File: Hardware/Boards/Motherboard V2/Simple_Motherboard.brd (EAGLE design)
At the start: 146.1 x 147.3 mm, 120 parts, among them J1 AVR_SPI_PRG_6PTH, U1 WIZ811MJ, U1_MUX 74HC4052D,653, U2 ATMEGA328P_PDIP, U2_MUX 74HC4052D,653, U3_MUX 74HC4052D,653, U4_MUX 74HC4052D,653, U5_MUX 74HC4052D,653, U7_MUX 74HC4052D,653, Y1 16MHz

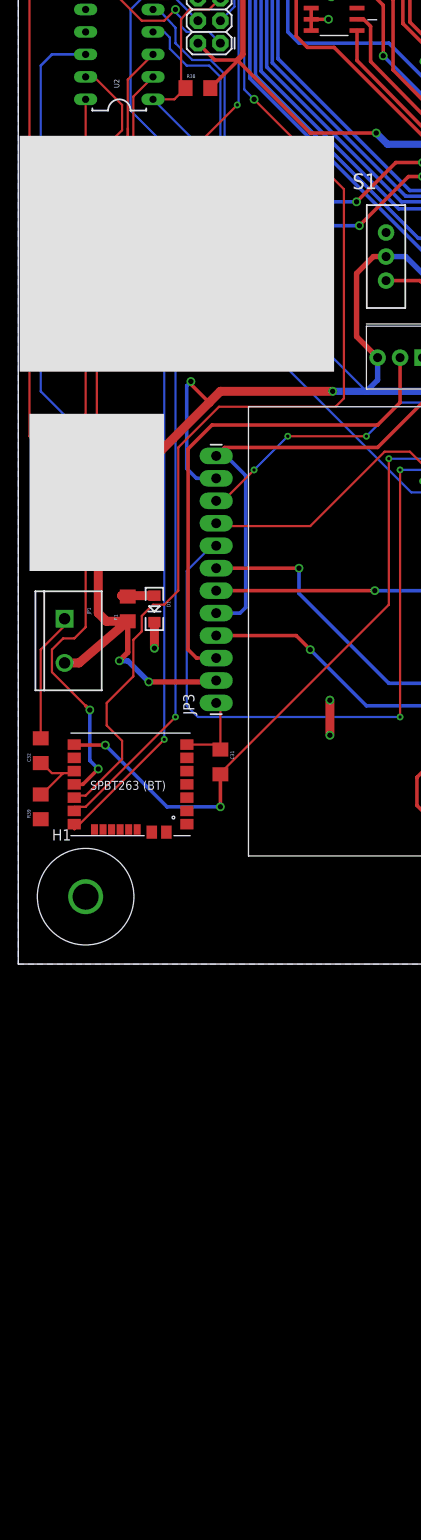
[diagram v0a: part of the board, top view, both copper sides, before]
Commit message: Removed sensor breakouts
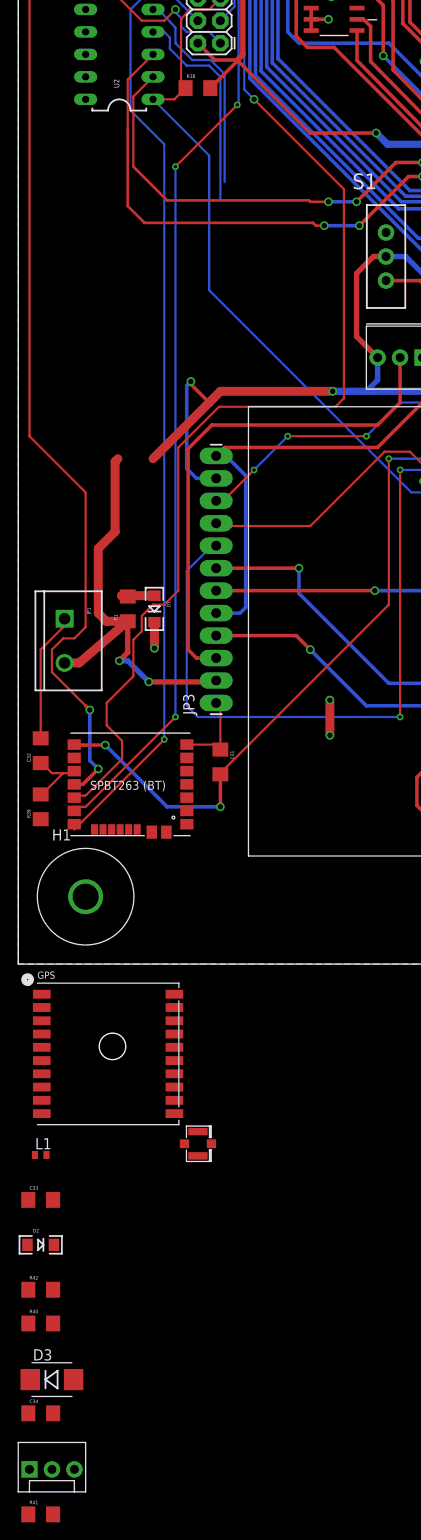
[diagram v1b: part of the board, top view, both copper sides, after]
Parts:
- removed JP2: (no value), SparkFun-Connectors:1X06_LONGPADS
- added C33: 1uF, SparkFun-Passives:1206
- added C34: .01uF, SparkFun-Passives:1206
- added D2: RED, SparkFun-LED:LED-1206
- added D3: (no value), SparkFun-DiscreteSemi:DIODE-HV
- added J2: U.FL, SparkFun-Connectors:U.FL
- added L1: BML15HB121SN1, inductors:0402
- added R40, R42: 1K, SparkFun-Passives:1206
- added R41: 10K, SparkFun-Passives:1206
- added TEMP: (no value), SparkFun-Connectors:MOLEX-1X3
- GPS: value M09 -> (none); device SparkFun-Connectors:1X09 -> adafruit:FGPMMOPA6H
- moved GPS 102.6 mm to (10.2, -10.2), turned to 0 degrees
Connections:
- removed net TMP_AL: JP2.4, U2.26
- removed net TMP_SCL: JP2.2, U2.28
- removed net TMP_SDA: JP2.1, U2.27
- new net N$23: D2.A, GPS.P$5
- new net N$24: D3.A, GPS.P$10, R40.1
- new net N$47: C33.1, C34.1, GPS.P$1, L1.2
- new net N$5: GPS.P$11, J2.P$3
- new net N$6: D2.C, R42.2
- new net TEMP: R41.1, TEMP.2, U2.23
- net +3V3: now also L1.1, R40.2
- net +5V: now also R41.2, TEMP.1; no longer GPS.8, JP2.5
- net GND: now also C33.2, C34.2, GPS.P$12, GPS.P$19, GPS.P$3, GPS.P$8, J2.P$1, J2.P$2, R42.1, TEMP.3; no longer GPS.7, JP2.6
- net GPS_RX: now also D3.C; no longer GPS.6
- net GPS_TX: now also GPS.P$9; no longer GPS.5
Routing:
- net TMP_SDA: track 59.6 -> 0.00 mm, vias 1 -> 0
- net TMP_AL: track 58.1 -> 0.00 mm
- net TMP_SCL: track 51.6 -> 0.00 mm, vias 1 -> 0
- net +5V: track 505.2 -> 490.5 mm
- net GPS_RX: track 37.0 -> 24.4 mm
- net GPS_TX: track 36.3 -> 24.4 mm

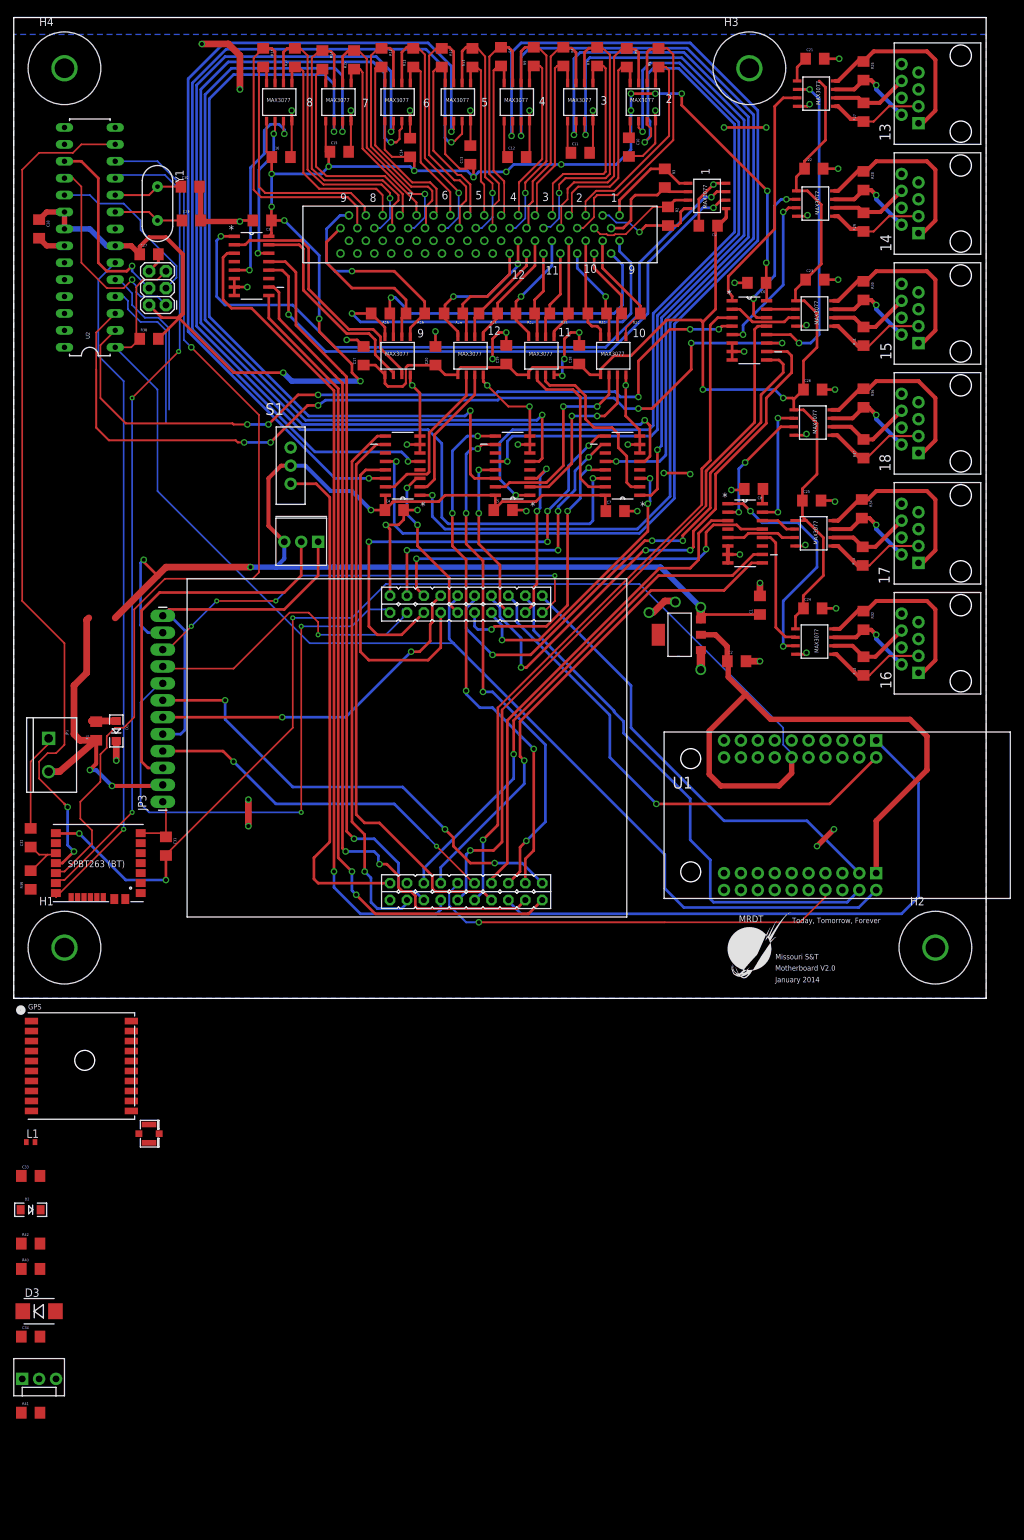
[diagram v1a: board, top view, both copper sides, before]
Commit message: Rewired LCD with 16 pin holes
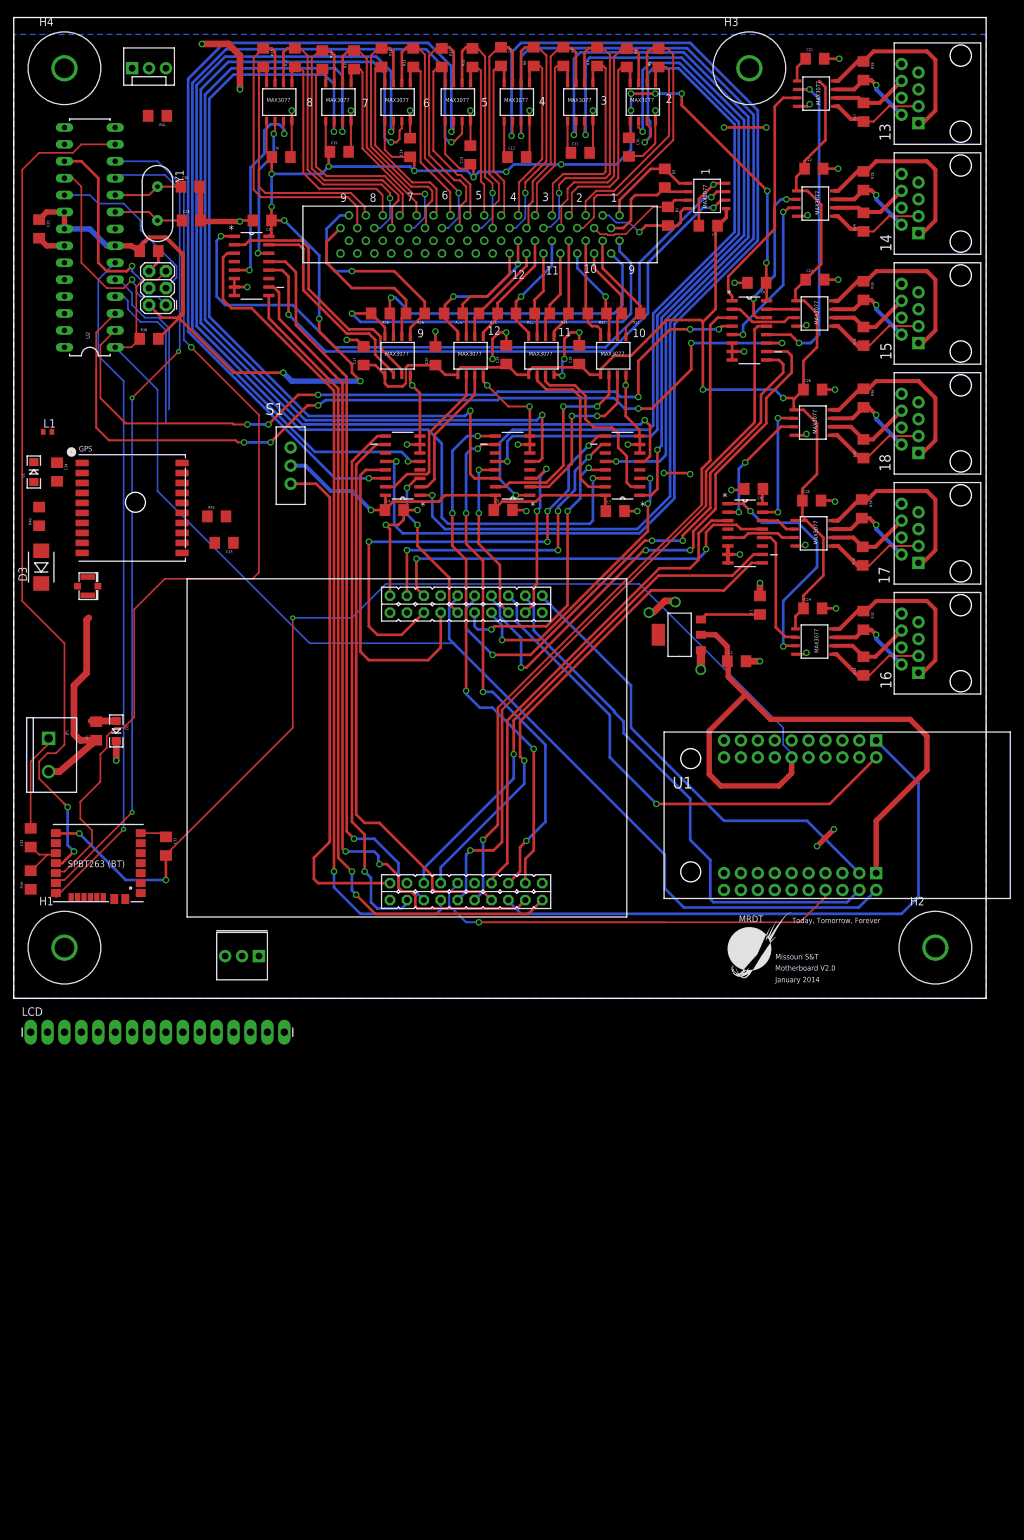
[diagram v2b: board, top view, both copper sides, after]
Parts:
- removed JP3: M12LONGPADS, SparkFun-Connectors:1X12_LONGPADS
- added LCD: M16LONGPADS, SparkFun-Connectors:1X16_LONGPADS
- moved TEMP 197.5 mm to (17.8, 139.7)
- moved R41 195.7 mm to (21.6, 132.6), turned to 180 degrees
- moved C34 129.9 mm to (6.51, 79.1), turned to 270 degrees
- moved R40 113.0 mm to (3.81, 72.4), turned to 90 degrees
- moved R42 112.7 mm to (30.5, 72.4)
- moved D3 111.8 mm to (4.13, 64.8), turned to 90 degrees
- moved D2 110.8 mm to (3.02, 79.1), turned to 90 degrees
- moved L1 106.7 mm to (5.08, 85.1)
- moved C33 99.4 mm to (31.6, 68.4), turned to 180 degrees
- moved GPS 84.2 mm to (17.8, 73.7)
- moved J2 82.7 mm to (11.1, 61.9)
- moved U$10 62.9 mm to (36.8, 8.89)
- moved C27 0.48 mm to (20.3, 112.2)
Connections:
- net +5V: now also LCD.15, LCD.2; no longer JP3.11, JP3.2
- net GND: now also LCD.1; no longer JP3.1
- net LCD_D4: now also LCD.11; no longer JP3.7
- net LCD_D5: now also LCD.12; no longer JP3.8
- net LCD_D6: now also LCD.13; no longer JP3.9
- net LCD_D7: now also LCD.14; no longer JP3.10
- net LCD_EN: now also LCD.6; no longer JP3.6
- net LCD_RS: now also LCD.4; no longer JP3.4
- net LCD_RW: now also LCD.16, LCD.5; no longer JP3.12, JP3.5
- net N$7: now also LCD.3; no longer JP3.3
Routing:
- net +5V: track 490.5 -> 342.3 mm, vias 23 -> 18
- net LCD_D5: track 86.8 -> 0.00 mm, vias 2 -> 0
- net LCD_D4: track 70.8 -> 0.00 mm, vias 3 -> 0
- net LCD_D7: track 70.1 -> 0.00 mm, vias 4 -> 0
- net N$7: track 57.5 -> 0.00 mm
- net LCD_RS: track 55.0 -> 0.00 mm, vias 2 -> 0
- net LCD_RW: track 53.7 -> 0.00 mm
- net LCD_EN: track 52.4 -> 0.00 mm, vias 2 -> 0
- net LCD_D6: track 45.2 -> 0.00 mm, vias 1 -> 0
- net GND: track 279.9 -> 270.9 mm, vias 60 -> 58

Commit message: Fixed some drc stuff
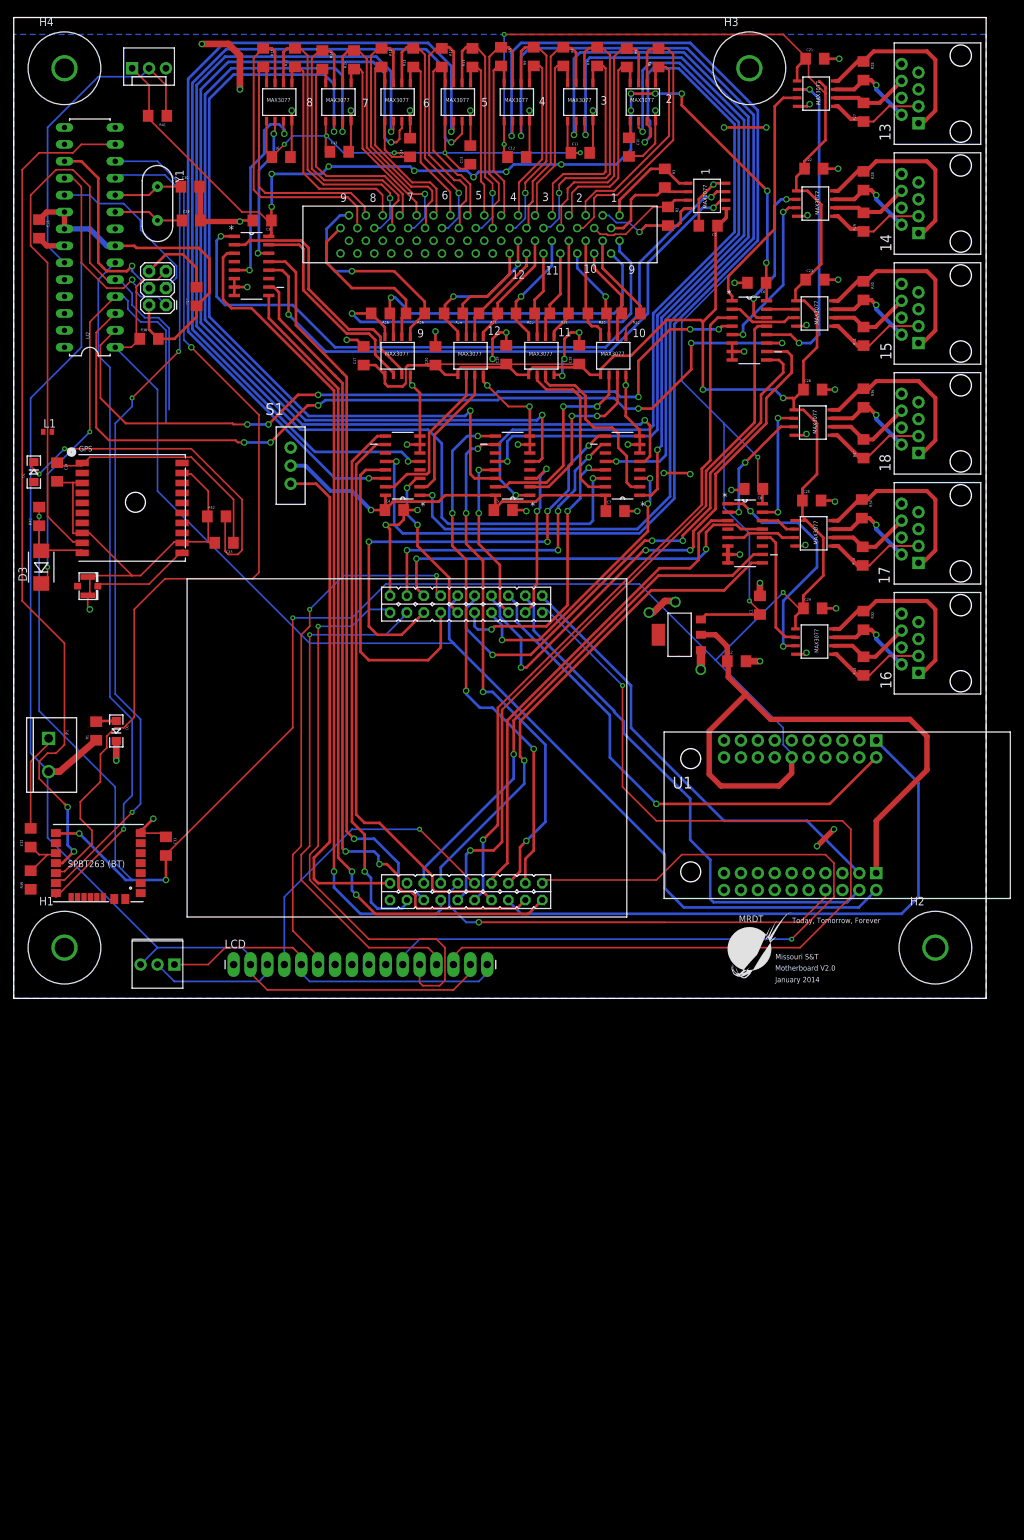
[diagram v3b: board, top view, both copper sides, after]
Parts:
- moved LCD 32.1 mm to (33.0, 5.08)
- moved U$10 12.8 mm to (24.1, 7.62)
- moved C27 9.88 mm to (27.5, 105.4), turned to 90 degrees
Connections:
- removed net LCD_RW: LCD.16, LCD.5, U$10.P$1
- net GND: now also LCD.16, LCD.5, U$10.P$1
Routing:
- net +3V3: track 509.6 -> 738.7 mm, vias 5 -> 14
- net +5V: track 342.3 -> 542.5 mm, vias 18 -> 16
- net LCD_D7: track 0.00 -> 143.9 mm, vias 0 -> 1
- net GND: track 270.9 -> 397.0 mm, vias 58 -> 60
- net LCD_D4: track 0.00 -> 120.9 mm, vias 0 -> 1
- net LCD_D5: track 0.00 -> 87.1 mm, vias 0 -> 1
- net GPS_TX: track 24.4 -> 108.4 mm
- net LCD_D6: track 0.00 -> 80.8 mm, vias 0 -> 1
- net LCD_EN: track 0.00 -> 80.5 mm, vias 0 -> 2
- net N$6: track 0.00 -> 53.7 mm, vias 0 -> 2
- net TEMP: track 0.00 -> 48.5 mm
- net GPS_RX: track 24.4 -> 72.8 mm, vias 0 -> 2
- net LCD_RS: track 0.00 -> 46.3 mm, vias 0 -> 1
- net N$47: track 0.00 -> 37.2 mm
- net N$7: track 0.00 -> 19.4 mm
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
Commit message: Moved a couple caps
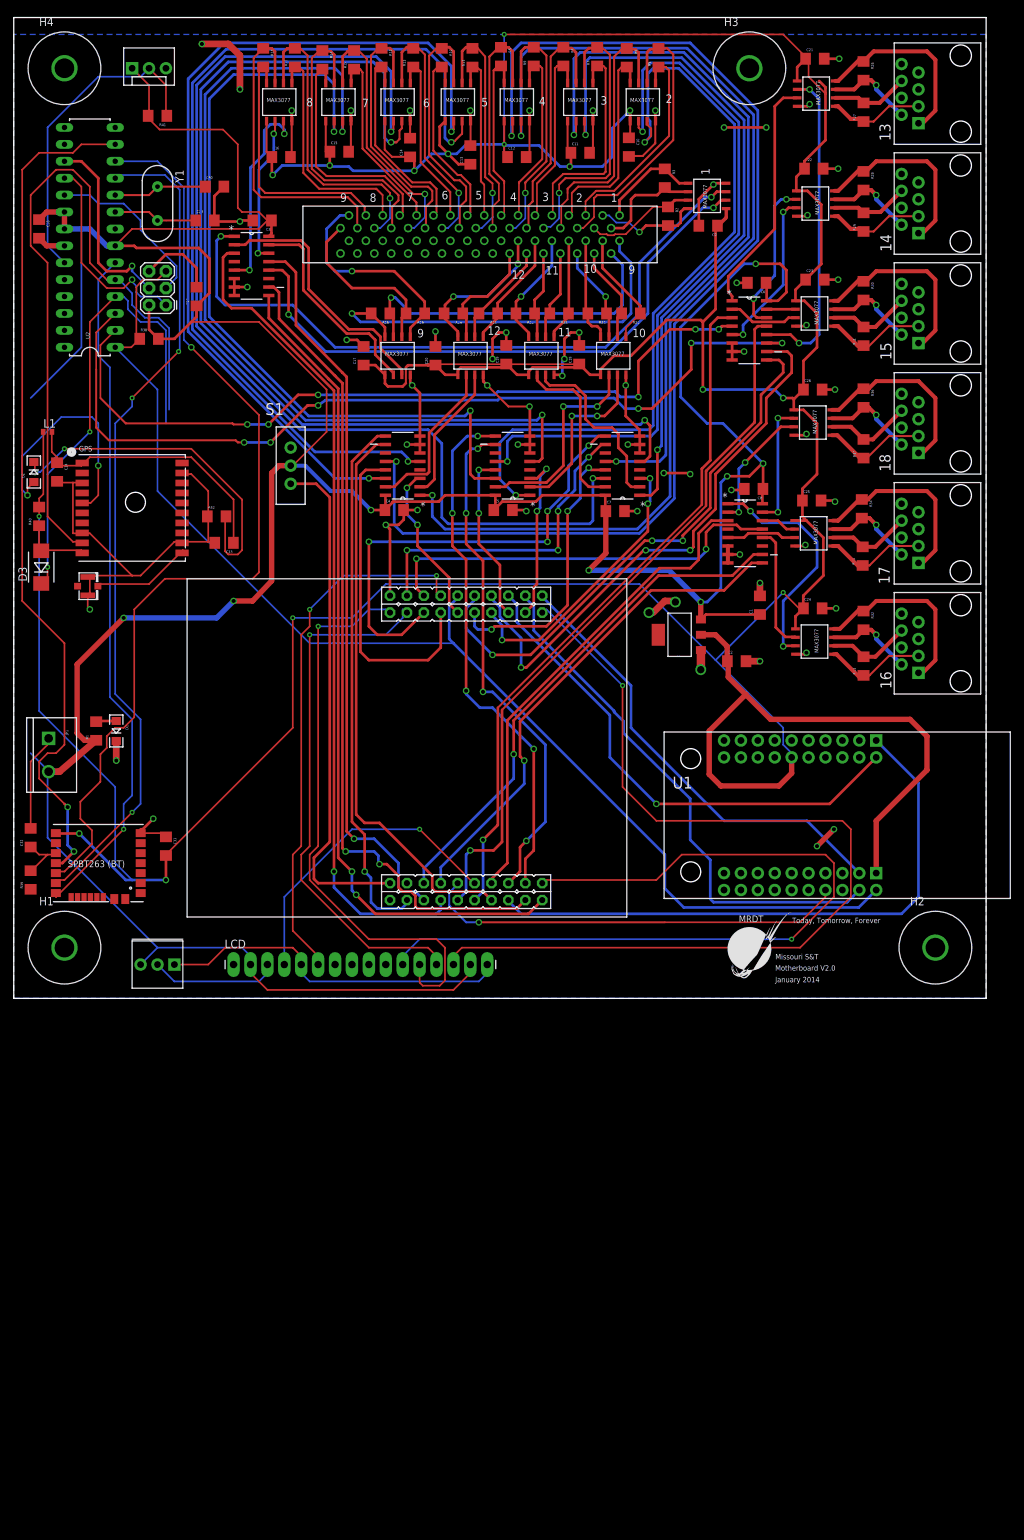
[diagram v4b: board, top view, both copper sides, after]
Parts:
- moved C30 3.65 mm to (30.2, 121.9)
- moved C29 2.06 mm to (28.7, 116.8)
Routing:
- net N$23: track 0.00 -> 36.5 mm, vias 0 -> 2
- net +3V3: track 738.7 -> 771.9 mm, vias 14 -> 15
- net N$47: track 37.2 -> 42.2 mm
- net +5V: track 542.5 -> 547.3 mm, vias 16 -> 8
- net ATCLK3: track 10.4 -> 14.0 mm
- net ATCLK4: track 10.6 -> 12.6 mm
- net GND: track 397.0 -> 396.5 mm
